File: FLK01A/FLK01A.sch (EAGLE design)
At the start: 29 parts, among them J1 M10SMD_MALE_SHORT, J2 M10SMD_MALE_SHORT, U1 LPC812TSSOP20, U2 EKMBTO5, U3 HTU21DSMD, U4 MMA8452Q, U5 VCNL4000, U6 MPL3115A2LGA8, Y1 12MHZ

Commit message: [flk/flr] adapt board layout to new M10 footprints + power switch
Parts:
- removed R6, R7: 4k7, SparkFun-Passives:RESISTOR0402-RES
- removed R8: 1k, SparkFun-Passives:RESISTOR0402-RES
- added U7: (no value), flukso:741G66
- R1, R2: value 100k -> 4k7
- R3: value 2M -> 100k
- R5: value 100k -> 1k
- U5: value VCNL4000 -> VCNL4010; device SparkFun-Sensors:VCNL4000 -> flukso:VCNL4010
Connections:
- new net VDD: C1.1, J2.5, U1.VDD, U7.VCC, U7.Y
- net !RESET!: no longer R1.1
- net 3.3V: now also U7.Z; no longer C1.1, J2.5, R3.2, R6.2, R7.2, U1.VDD
- net EKMB_INT: now also R3.2; no longer R4.2
- net GND: now also R3.1, U7.GND; no longer R5.1
- net I2C0_SCL: now also R1.1; no longer R6.1
- net I2C0_SDA: now also R2.1; no longer R7.1
- net ISP_RXD: now also R5.2; no longer R8.2
- net ISP_TXD: no longer R2.1
- net MMA_INT: now also R4.2; no longer R5.2
- net N$8: now also R5.1; no longer R8.1
- net PIO0_6: now also U7.E; no longer R3.1
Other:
- note added: "Copyright (c) 2015 Flukso"
- note removed: "Copyright (c) 2014 Flukso"
- moved on the sheet: C1, R1, R2, R3, R4, R5

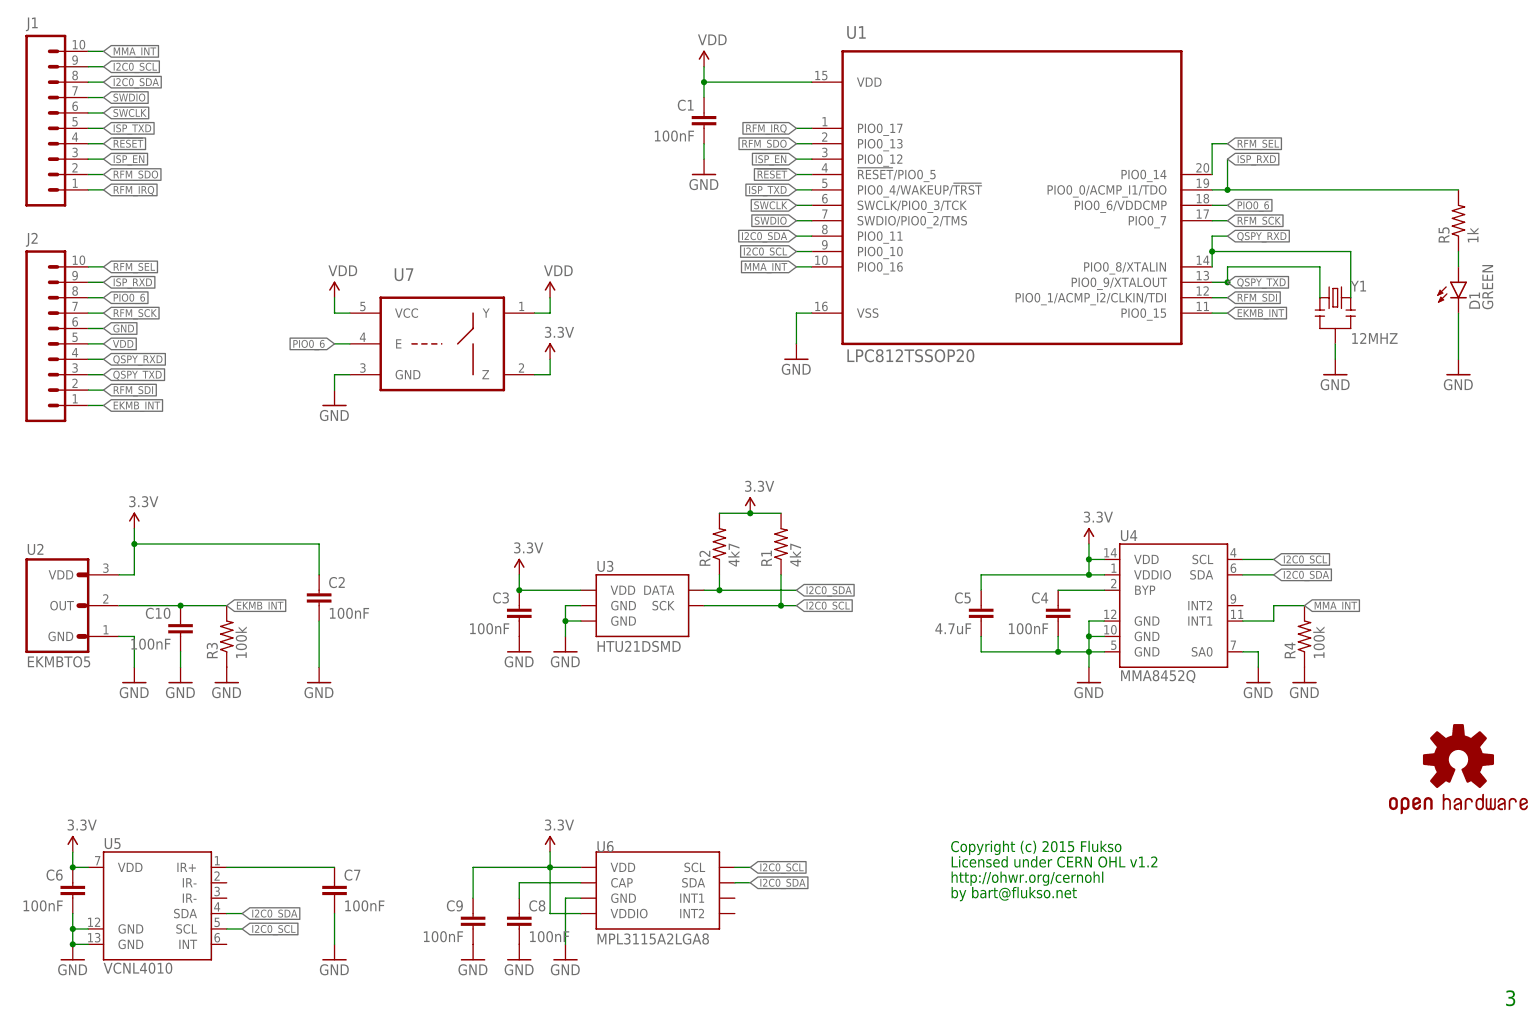
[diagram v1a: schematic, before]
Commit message: [flk] connect VCNL4010 int pin to LPC812
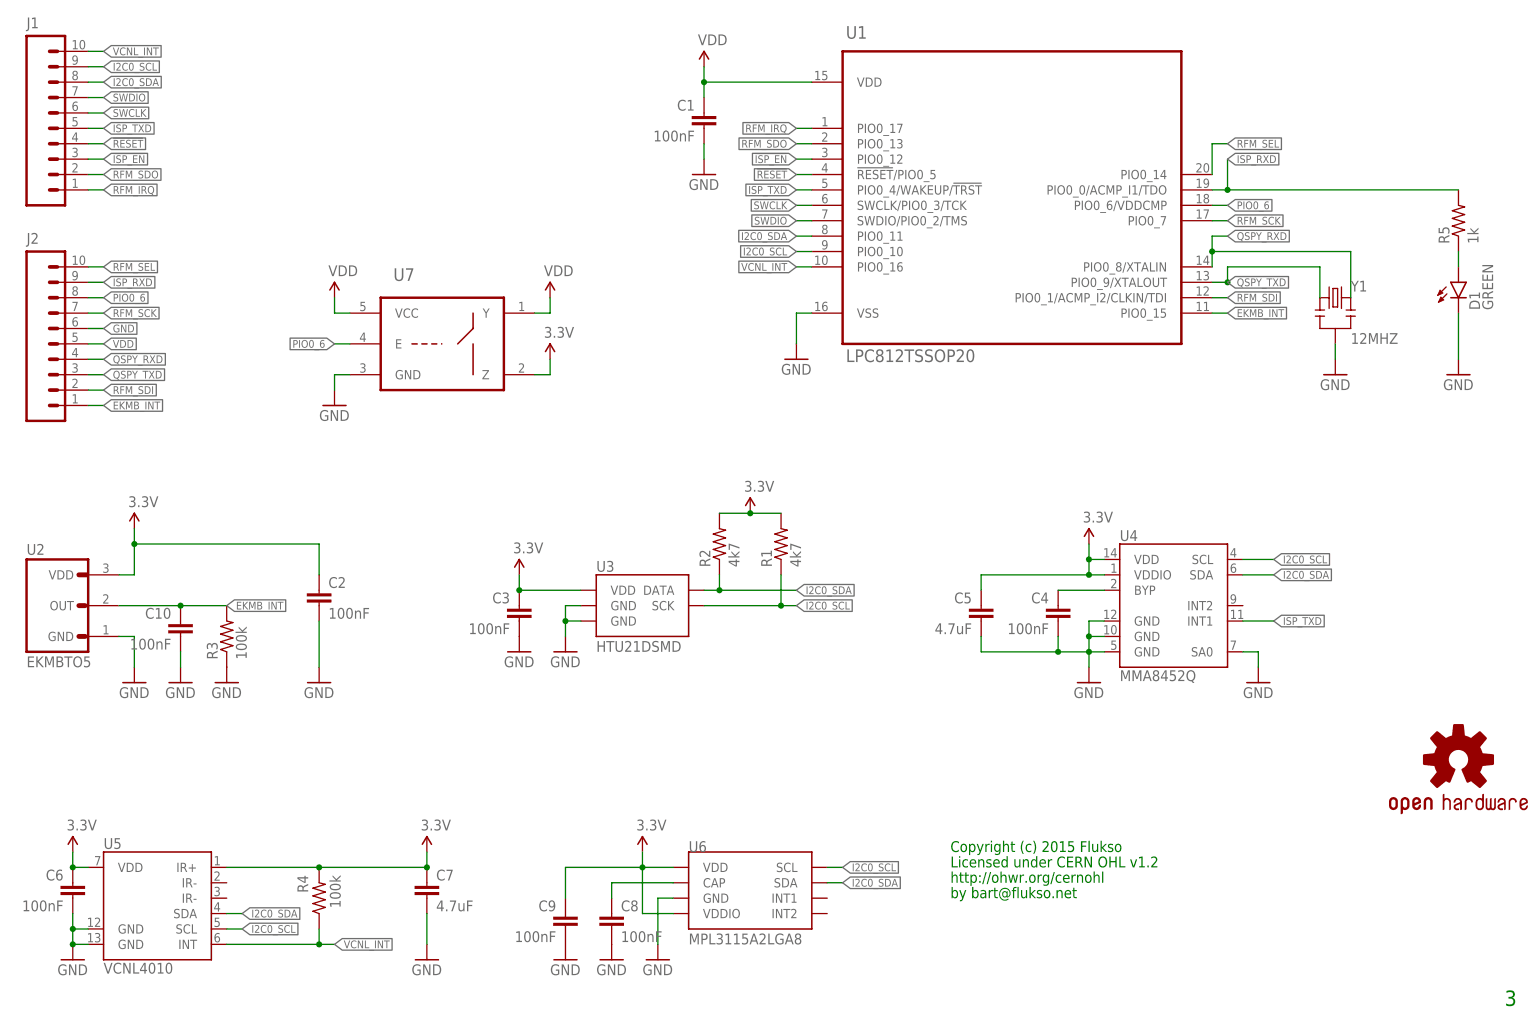
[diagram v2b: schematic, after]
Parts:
- C7: value 100nF -> 4.7uF; device flukso:CAP0402-CAP -> flukso:CAP0805-CAP
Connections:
- removed net MMA_INT: J1.10, R4.2, U1.PIO0_16, U4.INT1
- removed net N$1: C7.1, U5.IR+
- new net VCNL_INT: J1.10, R4.1, U1.PIO0_16, U5.INT
- net 3.3V: now also C7.1, R4.2, U5.IR+
- net GND: no longer R4.1
- net ISP_TXD: now also U4.INT1
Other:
- moved on the sheet: C7, C8, C9, R4, U6
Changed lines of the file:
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@@
 <part name="C4" library="flukso" deviceset="CAP" device="0402-CAP" value="100nF"/>
 <part name="GND10" library="SparkFun-Aesthetics" deviceset="GND" device=""/>
-<part name="R4" library="SparkFun-Passives" deviceset="RESISTOR" device="0402-RES" value="100k"/>
-<part name="GND11" library="SparkFun-Aesthetics" deviceset="GND" device=""/>
 <part name="SUPPLY7" library="SparkFun-Aesthetics" deviceset="3.3V" device=""/>
 <part name="GND12" library="SparkFun-Aesthetics" deviceset="GND" device=""/>
 <part name="C6" library="flukso" deviceset="CAP" device="0402-CAP" value="100nF"/>
-<part name="C7" library="flukso" deviceset="CAP" device="0402-CAP" value="100nF"/>
 <part name="GND13" library="SparkFun-Aesthetics" deviceset="GND" device=""/>
 <part name="U6" library="SparkFun-Sensors" deviceset="MPL3115A2" device="LGA8"/>
@@
 <part name="GND19" library="SparkFun-Aesthetics" deviceset="GND" device=""/>
 <part name="U5" library="flukso" deviceset="VCNL4010" device=""/>
+<part name="C7" library="flukso" deviceset="CAP" device="0805-CAP" value="4.7uF"/>
+<part name="SUPPLY11" library="SparkFun-Aesthetics" deviceset="3.3V" device=""/>
+<part name="R4" library="SparkFun-Passives" deviceset="RESISTOR" device="0402-RES" value="100k"/>
 </parts>
 <sheets>
@@
 <instance part="C4" gate="G$1" x="182.88" y="71.12" rot="MR0"/>
 <instance part="GND10" gate="1" x="215.9" y="60.96"/>
-<instance part="R4" gate="G$1" x="223.52" y="68.58" rot="R90"/>
-<instance part="GND11" gate="1" x="223.52" y="60.96"/>
 <instance part="SUPPLY7" gate="G$1" x="20.32" y="33.02"/>
 <instance part="GND12" gate="1" x="20.32" y="15.24"/>
 <instance part="C6" gate="G$1" x="20.32" y="25.4" rot="MR0"/>
-<instance part="C7" gate="G$1" x="63.5" y="25.4"/>
-<instance part="GND13" gate="1" x="63.5" y="15.24"/>
-<instance part="U6" gate="G$1" x="116.84" y="27.94"/>
-<instance part="SUPPLY8" gate="G$1" x="99.06" y="33.02"/>
-<instance part="GND14" gate="1" x="93.98" y="15.24"/>
-<instance part="C8" gate="G$1" x="93.98" y="20.32"/>
-<instance part="C9" gate="G$1" x="86.36" y="20.32" rot="MR0"/>
-<instance part="GND15" gate="1" x="86.36" y="15.24"/>
-<instance part="GND16" gate="1" x="101.6" y="15.24"/>
+<instance part="GND13" gate="1" x="78.74" y="15.24"/>
+<instance part="U6" gate="G$1" x="132.08" y="27.94"/>
+<instance part="SUPPLY8" gate="G$1" x="114.3" y="33.02"/>
+<instance part="GND14" gate="1" x="109.22" y="15.24"/>
+<instance part="C8" gate="G$1" x="109.22" y="20.32"/>
+<instance part="C9" gate="G$1" x="101.6" y="20.32" rot="MR0"/>
+<instance part="GND15" gate="1" x="101.6" y="15.24"/>
+<instance part="GND16" gate="1" x="116.84" y="15.24"/>
 <instance part="D1" gate="G$1" x="248.92" y="127"/>
 <instance part="R5" gate="G$1" x="248.92" y="137.16" rot="R90"/>
@@
 <instance part="GND19" gate="1" x="63.5" y="106.68"/>
 <instance part="U5" gate="G$1" x="33.02" y="25.4"/>
+<instance part="C7" gate="G$1" x="78.74" y="25.4"/>
+<instance part="SUPPLY11" gate="G$1" x="78.74" y="33.02"/>
+<instance part="R4" gate="G$1" x="60.96" y="25.4" smashed="yes" rot="R90">
+<attribute name="NAME" x="57.3786" y="29.21" size="1.778" layer="95" rot="R270"/>
+<attribute name="VALUE" x="62.738" y="29.21" size="1.778" layer="96" rot="R270"/>
+</instance>
 </instances>
 <busses>
@@
 </segment>
 <segment>
+<pinref part="GND13" gate="1" pin="GND"/>
+<wire x1="78.74" y1="22.86" x2="78.74" y2="17.78" width="0.1524" layer="91"/>
 <pinref part="C7" gate="G$1" pin="2"/>
-<pinref part="GND13" gate="1" pin="GND"/>
-<wire x1="63.5" y1="22.86" x2="63.5" y2="17.78" width="0.1524" layer="91"/>
 </segment>
 <segment>
@@
 </segment>
 <segment>
-<pinref part="R4" gate="G$1" pin="1"/>
-<pinref part="GND11" gate="1" pin="GND"/>
-</segment>
-<segment>
 <pinref part="U6" gate="G$1" pin="GND"/>
 <pinref part="GND16" gate="1" pin="GND"/>
-<wire x1="104.14" y1="25.4" x2="101.6" y2="25.4" width="0.1524" layer="91"/>
-<wire x1="101.6" y1="25.4" x2="101.6" y2="17.78" width="0.1524" layer="91"/>
+<wire x1="119.38" y1="25.4" x2="116.84" y2="25.4" width="0.1524" layer="91"/>
+<wire x1="116.84" y1="25.4" x2="116.84" y2="17.78" width="0.1524" layer="91"/>
 </segment>
 <segment>
@@
 <label x="25.4" y="152.4" size="1.27" layer="95" xref="yes"/>
 <pinref part="J1" gate="G$1" pin="5"/>
+</segment>
+<segment>
+<pinref part="U4" gate="G$1" pin="INT1"/>
+<wire x1="213.36" y1="71.12" x2="218.44" y2="71.12" width="0.1524" layer="91"/>
+<label x="218.44" y="71.12" size="1.27" layer="95" xref="yes"/>
 </segment>
 </net>
@@
 <segment>
 <pinref part="U6" gate="G$1" pin="SDA"/>
-<wire x1="129.54" y1="27.94" x2="132.08" y2="27.94" width="0.1524" layer="91"/>
-<label x="132.08" y="27.94" size="1.27" layer="95" xref="yes"/>
+<wire x1="144.78" y1="27.94" x2="147.32" y2="27.94" width="0.1524" layer="91"/>
+<label x="147.32" y="27.94" size="1.27" layer="95" xref="yes"/>
 </segment>
 <segment>
@@
 <segment>
 <pinref part="U6" gate="G$1" pin="SCL"/>
-<wire x1="129.54" y1="30.48" x2="132.08" y2="30.48" width="0.1524" layer="91"/>
-<label x="132.08" y="30.48" size="1.27" layer="95" xref="yes"/>
+<wire x1="144.78" y1="30.48" x2="147.32" y2="30.48" width="0.1524" layer="91"/>
+<label x="147.32" y="30.48" size="1.27" layer="95" xref="yes"/>
 </segment>
 <segment>
@@
 <wire x1="22.86" y1="162.56" x2="25.4" y2="162.56" width="0.1524" layer="91"/>
 <label x="25.4" y="162.56" size="1.27" layer="95" xref="yes"/>
-</segment>
-</net>
-<net name="MMA_INT" class="0">
-<segment>
-<pinref part="U1" gate="A" pin="PIO0_16"/>
-<wire x1="142.24" y1="129.54" x2="139.7" y2="129.54" width="0.1524" layer="91"/>
-<label x="139.7" y="129.54" size="1.27" layer="95" rot="R180" xref="yes"/>
-</segment>
-<segment>
-<wire x1="22.86" y1="165.1" x2="25.4" y2="165.1" width="0.1524" layer="91"/>
-<label x="25.4" y="165.1" size="1.27" layer="95" xref="yes"/>
-<pinref part="J1" gate="G$1" pin="10"/>
-</segment>
-<segment>
-<pinref part="U4" gate="G$1" pin="INT1"/>
-<wire x1="213.36" y1="71.12" x2="218.44" y2="71.12" width="0.1524" layer="91"/>
-<wire x1="218.44" y1="71.12" x2="218.44" y2="73.66" width="0.1524" layer="91"/>
-<pinref part="R4" gate="G$1" pin="2"/>
-<wire x1="218.44" y1="73.66" x2="223.52" y2="73.66" width="0.1524" layer="91"/>
-<label x="223.52" y="73.66" size="1.27" layer="95" xref="yes"/>
 </segment>
 </net>
@@
 <pinref part="SUPPLY8" gate="G$1" pin="3.3V"/>
 <pinref part="U6" gate="G$1" pin="VDD"/>
-<wire x1="99.06" y1="33.02" x2="99.06" y2="30.48" width="0.1524" layer="91"/>
-<wire x1="99.06" y1="30.48" x2="104.14" y2="30.48" width="0.1524" layer="91"/>
+<wire x1="114.3" y1="33.02" x2="114.3" y2="30.48" width="0.1524" layer="91"/>
+<wire x1="114.3" y1="30.48" x2="119.38" y2="30.48" width="0.1524" layer="91"/>
 <pinref part="U6" gate="G$1" pin="VDDIO"/>
-<wire x1="104.14" y1="22.86" x2="99.06" y2="22.86" width="0.1524" layer="91"/>
-<wire x1="99.06" y1="22.86" x2="99.06" y2="30.48" width="0.1524" layer="91"/>
-<junction x="99.06" y="30.48"/>
+<wire x1="119.38" y1="22.86" x2="114.3" y2="22.86" width="0.1524" layer="91"/>
+<wire x1="114.3" y1="22.86" x2="114.3" y2="30.48" width="0.1524" layer="91"/>
+<junction x="114.3" y="30.48"/>
 <pinref part="C9" gate="G$1" pin="1"/>
-<wire x1="99.06" y1="30.48" x2="86.36" y2="30.48" width="0.1524" layer="91"/>
-<wire x1="86.36" y1="30.48" x2="86.36" y2="25.4" width="0.1524" layer="91"/>
+<wire x1="114.3" y1="30.48" x2="101.6" y2="30.48" width="0.1524" layer="91"/>
+<wire x1="101.6" y1="30.48" x2="101.6" y2="25.4" width="0.1524" layer="91"/>
 </segment>
 <segment>
@@
 <wire x1="96.52" y1="111.76" x2="99.06" y2="111.76" width="0.1524" layer="91"/>
 <wire x1="99.06" y1="111.76" x2="99.06" y2="114.3" width="0.1524" layer="91"/>
+</segment>
+<segment>
+<wire x1="45.72" y1="30.48" x2="60.96" y2="30.48" width="0.1524" layer="91"/>
+<pinref part="U5" gate="G$1" pin="IR+"/>
+<pinref part="C7" gate="G$1" pin="1"/>
+<pinref part="SUPPLY11" gate="G$1" pin="3.3V"/>
+<wire x1="60.96" y1="30.48" x2="78.74" y2="30.48" width="0.1524" layer="91"/>
+<wire x1="78.74" y1="33.02" x2="78.74" y2="30.48" width="0.1524" layer="91"/>
+<junction x="78.74" y="30.48"/>
+<pinref part="R4" gate="G$1" pin="2"/>
+<junction x="60.96" y="30.48"/>
 </segment>
 </net>
@@
 </segment>
 </net>
-<net name="N$1" class="0">
-<segment>
-<pinref part="C7" gate="G$1" pin="1"/>
-<wire x1="45.72" y1="30.48" x2="63.5" y2="30.48" width="0.1524" layer="91"/>
-<pinref part="U5" gate="G$1" pin="IR+"/>
-</segment>
-</net>
 <net name="N$6" class="0">
 <segment>
 <pinref part="C8" gate="G$1" pin="1"/>
 <pinref part="U6" gate="G$1" pin="CAP"/>
-<wire x1="93.98" y1="25.4" x2="93.98" y2="27.94" width="0.1524" layer="91"/>
-<wire x1="93.98" y1="27.94" x2="104.14" y2="27.94" width="0.1524" layer="91"/>
+<wire x1="109.22" y1="25.4" x2="109.22" y2="27.94" width="0.1524" layer="91"/>
+<wire x1="109.22" y1="27.94" x2="119.38" y2="27.94" width="0.1524" layer="91"/>
 </segment>
 </net>
@@
 </segment>
 </net>
+<net name="VCNL_INT" class="0">
+<segment>
+<pinref part="U1" gate="A" pin="PIO0_16"/>
+<wire x1="142.24" y1="129.54" x2="139.7" y2="129.54" width="0.1524" layer="91"/>
+<label x="139.7" y="129.54" size="1.27" layer="95" rot="R180" xref="yes"/>
+</segment>
+<segment>
+<pinref part="U5" gate="G$1" pin="INT"/>
+<wire x1="45.72" y1="17.78" x2="60.96" y2="17.78" width="0.1524" layer="91"/>
+<label x="63.5" y="17.78" size="1.27" layer="95" xref="yes"/>
+<pinref part="R4" gate="G$1" pin="1"/>
+<wire x1="60.96" y1="17.78" x2="63.5" y2="17.78" width="0.1524" layer="91"/>
+<wire x1="60.96" y1="20.32" x2="60.96" y2="17.78" width="0.1524" layer="91"/>
+<junction x="60.96" y="17.78"/>
+</segment>
+<segment>
+<pinref part="J1" gate="G$1" pin="10"/>
+<wire x1="22.86" y1="165.1" x2="25.4" y2="165.1" width="0.1524" layer="91"/>
+<label x="25.4" y="165.1" size="1.27" layer="95" xref="yes"/>
+</segment>
+</net>
